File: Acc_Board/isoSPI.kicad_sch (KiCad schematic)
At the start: 11 parts, among them J2 IsoSPI

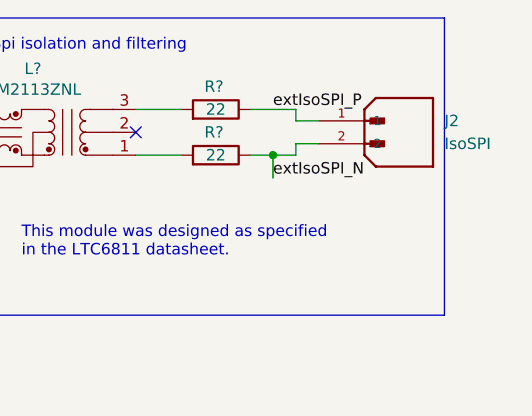
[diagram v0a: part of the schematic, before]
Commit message: Fixed crossover traces for SPI on acc board
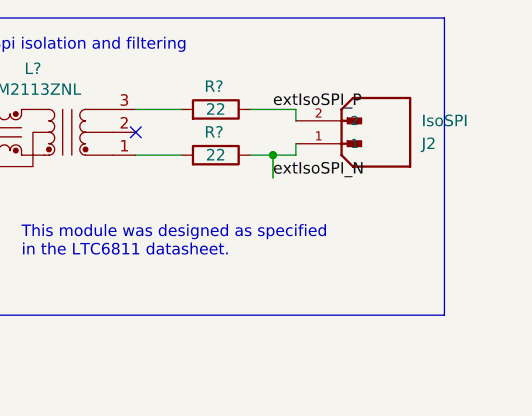
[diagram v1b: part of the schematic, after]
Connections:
- net extIsoSPI_N: now also J2.1; no longer J2.2
- net extIsoSPI_P: now also J2.2; no longer J2.1
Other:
- moved on the sheet: J2
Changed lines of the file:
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@@
-    (stroke (width 0) (type default))
-  )
-  (wire (pts (xy 166.37 33.02) (xy 168.91 33.02))
     (stroke (width 0) (type default))
   )
   (wire (pts (xy 121.92 36.83) (xy 121.92 41.91))
-    (stroke (width 0) (type default))
-  )
-  (wire (pts (xy 166.37 35.56) (xy 168.91 35.56))
     (stroke (width 0) (type default))
   )
@@
     )
   )
-  (symbol (lib_id "1FS_2_Global_Symbol_Library:1053091202") (at 173.99 33.02 0) (unit 1)
-    (in_bom yes) (on_board yes) (dnp no) (fields_autoplaced)
-    (property "Reference" "J2" (at 182.88 33.02 0)
-      (effects (font (size 1.27 1.27)) (justify left))
-    )
-    (property "Value" "IsoSPI" (at 182.88 35.56 0)
-      (effects (font (size 1.27 1.27)) (justify left))
-    )
-    (property "Footprint" "1FS_2_Global_Footprint_Library:MOLEX_1053091202" (at 173.99 33.02 0)
+  (symbol (lib_id "1FS_2_Global_Symbol_Library:1053091202") (at 171.45 35.56 0) (mirror x) (unit 1)
+    (in_bom yes) (on_board yes) (dnp no)
+    (property "Reference" "J2" (at 180.34 35.56 0)
+      (effects (font (size 1.27 1.27)) (justify left))
+    )
+    (property "Value" "IsoSPI" (at 180.34 33.02 0)
+      (effects (font (size 1.27 1.27)) (justify left))
+    )
+    (property "Footprint" "1FS_2_Global_Footprint_Library:MOLEX_1053091202" (at 171.45 35.56 0)
       (effects (font (size 1.27 1.27)) (justify bottom) hide)
     )
-    (property "Datasheet" "" (at 173.99 33.02 0)
-      (effects (font (size 1.27 1.27)) hide)
-    )
-    (property "PARTREV" "H" (at 173.99 33.02 0)
+    (property "Datasheet" "" (at 171.45 35.56 0)
+      (effects (font (size 1.27 1.27)) hide)
+    )
+    (property "PARTREV" "H" (at 171.45 35.56 0)
       (effects (font (size 1.27 1.27)) (justify bottom) hide)
     )
-    (property "STANDARD" "Manufacturer Recommendations" (at 173.99 33.02 0)
+    (property "STANDARD" "Manufacturer Recommendations" (at 171.45 35.56 0)
       (effects (font (size 1.27 1.27)) (justify bottom) hide)
     )
-    (property "MAXIMUM_PACKAGE_HEIGHT" "10.51 mm" (at 173.99 33.02 0)
+    (property "MAXIMUM_PACKAGE_HEIGHT" "10.51 mm" (at 171.45 35.56 0)
       (effects (font (size 1.27 1.27)) (justify bottom) hide)
     )
-    (property "MANUFACTURER" "Molex" (at 173.99 33.02 0)
+    (property "MANUFACTURER" "Molex" (at 171.45 35.56 0)
       (effects (font (size 1.27 1.27)) (justify bottom) hide)
     )

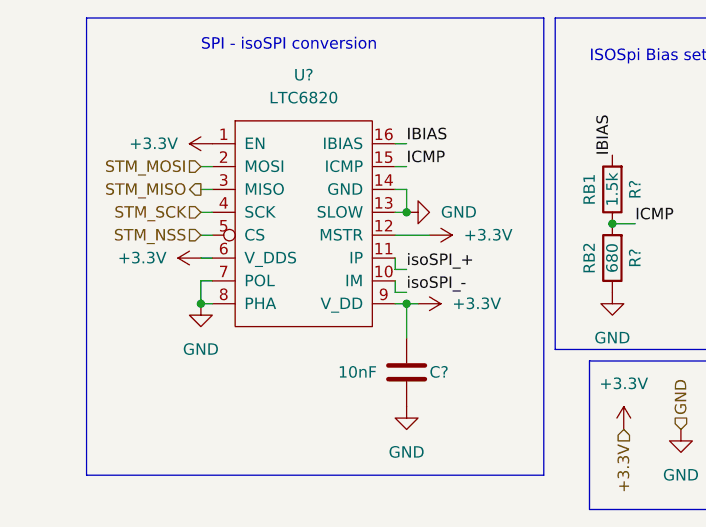
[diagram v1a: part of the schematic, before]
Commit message: acc board bms miso pull up resistor
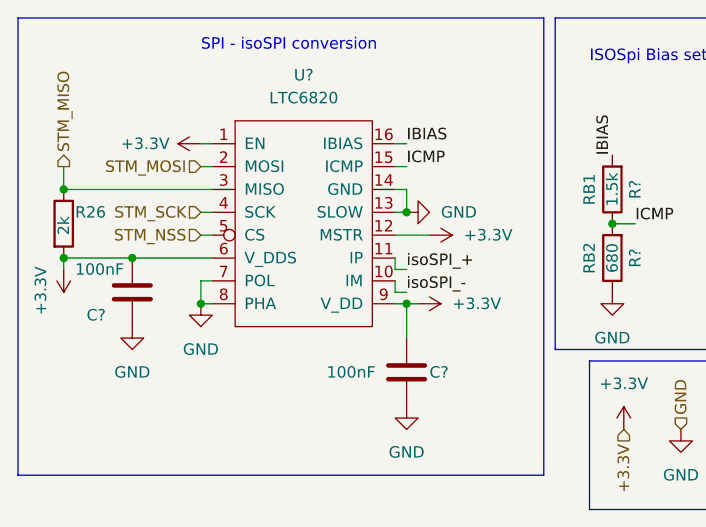
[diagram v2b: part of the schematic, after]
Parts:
- added C?: 100nF, Capacitor_SMD:C_0805_2012Metric_Pad1.18x1.45mm_HandSolder, symbol Device:C
- added R26: 2k, symbol Device:R
- C?: value 10nF -> 100nF
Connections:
- net +3.3V: now also C?.1, R26.2
- net GND: now also C?.2
- net STM_MISO: now also R26.1
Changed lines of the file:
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@@
 (kicad_sch (version 20230121) (generator eeschema)
   (paper "A4")
+  (junction (at 20.32 48.26) (diameter 0) (color 0 0 0 0)
+  )
   (junction (at 163.83 36.83) (diameter 0) (color 0 0 0 0)
   )
   (junction (at 116.84 26.67) (diameter 0) (color 0 0 0 0)
   )
+  (junction (at 20.32 40.64) (diameter 0) (color 0 0 0 0)
+  )
   (junction (at 58.42 53.34) (diameter 0) (color 0 0 0 0)
   )
@@
   )
   (junction (at 116.84 41.91) (diameter 0) (color 0 0 0 0)
+  )
+  (junction (at 27.94 48.26) (diameter 0) (color 0 0 0 0)
   )
   (no_connect (at 148.59 34.29))
@@
     (stroke (width 0) (type default))
   )
-  (wire (pts (xy 35.56 40.64) (xy 36.83 40.64))
+  (wire (pts (xy 20.32 40.64) (xy 36.83 40.64))
     (stroke (width 0) (type default))
   )
@@
     (stroke (width 0) (type default))
   )
+  (wire (pts (xy 35.56 35.56) (xy 36.83 35.56))
+    (stroke (width 0) (type default))
+  )
+  (wire (pts (xy 27.94 48.26) (xy 36.83 48.26))
+    (stroke (width 0) (type default))
+  )
   (polyline (pts (xy 101.6 54.61) (xy 101.6 21.59))
     (stroke (width 0) (type default))
@@
     (stroke (width 0) (type default))
   )
+  (wire (pts (xy 20.32 38.1) (xy 20.32 40.64))
+    (stroke (width 0) (type default))
+  )
   (wire (pts (xy 58.42 35.56) (xy 57.15 35.56))
     (stroke (width 0) (type default))
@@
     (stroke (width 0) (type default))
   )
-  (wire (pts (xy 35.56 48.26) (xy 36.83 48.26))
+  (wire (pts (xy 20.32 48.26) (xy 27.94 48.26))
     (stroke (width 0) (type default))
   )
@@
     (stroke (width 0) (type default))
   )
+  (wire (pts (xy 20.32 49.53) (xy 20.32 48.26))
+    (stroke (width 0) (type default))
+  )
   (wire (pts (xy 58.42 38.1) (xy 57.15 38.1))
     (stroke (width 0) (type default))
@@
     (stroke (width 0) (type default))
   )
-  (rectangle (start 22.86 21.59) (end 73.66 72.39)
+  (rectangle (start 15.24 21.59) (end 73.66 72.39)
     (stroke (width 0) (type default))
     (fill (type none))
@@
     (effects (font (size 1.27 1.27)) (justify right))
   )
-  (hierarchical_label "STM_MISO" (shape output) (at 35.56 40.64 180) (fields_autoplaced)
-    (effects (font (size 1.27 1.27)) (justify right))
+  (hierarchical_label "STM_MISO" (shape output) (at 20.32 38.1 90) (fields_autoplaced)
+    (effects (font (size 1.27 1.27)) (justify left))
   )
   (hierarchical_label "STM_MOSI" (shape input) (at 35.56 38.1 180) (fields_autoplaced)
@@
     )
   )
+  (symbol (lib_id "Device:C") (at 27.94 52.07 0) (unit 1)
+    (in_bom yes) (on_board yes) (dnp no)
+    (property "Reference" "C?" (at 22.86 54.61 0)
+      (effects (font (size 1.27 1.27)) (justify left))
+    )
+    (property "Value" "100nF" (at 21.59 49.53 0)
+      (effects (font (size 1.27 1.27)) (justify left))
+    )
+    (property "Footprint" "Capacitor_SMD:C_0805_2012Metric_Pad1.18x1.45mm_HandSolder" (at 28.9052 55.88 0)
+      (effects (font (size 1.27 1.27)) hide)
+    )
+    (property "Datasheet" "~" (at 27.94 52.07 0)
+      (effects (font (size 1.27 1.27)) hide)
+    )
+    (pin "1")
+    (pin "2")
+    (instances
+      (project "BMS_Controller"
+        (path "/cb6c61fd-673a-449c-8134-4a1c25621518"
+          (reference "C?") (unit 1)
+        )
+        (path "/cb6c61fd-673a-449c-8134-4a1c25621518/faa386f8-35fb-44d9-8ccf-12944498b7dc"
+          (reference "C?") (unit 1)
+        )
+      )
+      (project "Acc_Board"
+        (path "/e19d26dd-723b-45e6-9d59-b1730158e759/418586a7-bc6a-480e-8435-4a2eb96d1e0c"
+          (reference "C18") (unit 1)
+        )
+      )
+    )
+  )
   (symbol (lib_id "FSSymbols:HM2113ZNL") (at 137.16 34.29 0) (unit 1)
     (in_bom yes) (on_board yes) (dnp no)
@@
     )
   )
-  (symbol (lib_id "power:+3.3V") (at 35.56 48.26 90) (unit 1)
-    (in_bom yes) (on_board yes) (dnp no) (fields_autoplaced)
-    (property "Reference" "#PWR?" (at 39.37 48.26 0)
-      (effects (font (size 1.27 1.27)) hide)
-    )
-    (property "Value" "+3.3V" (at 31.75 48.26 90)
-      (effects (font (size 1.27 1.27)) (justify left))
-    )
-    (property "Footprint" "" (at 35.56 48.26 0)
-      (effects (font (size 1.27 1.27)) hide)
-    )
-    (property "Datasheet" "" (at 35.56 48.26 0)
+  (symbol (lib_id "power:+3.3V") (at 20.32 49.53 180) (unit 1)
+    (in_bom yes) (on_board yes) (dnp no)
+    (property "Reference" "#PWR?" (at 20.32 45.72 0)
+      (effects (font (size 1.27 1.27)) hide)
+    )
+    (property "Value" "+3.3V" (at 17.78 54.61 90)
+      (effects (font (size 1.27 1.27)) (justify right))
+    )
+    (property "Footprint" "" (at 20.32 49.53 0)
+      (effects (font (size 1.27 1.27)) hide)
+    )
+    (property "Datasheet" "" (at 20.32 49.53 0)
       (effects (font (size 1.27 1.27)) hide)
     )
@@
     )
   )
+  (symbol (lib_id "power:GND") (at 27.94 55.88 0) (unit 1)
+    (in_bom yes) (on_board yes) (dnp no) (fields_autoplaced)
+    (property "Reference" "#PWR055" (at 27.94 62.23 0)
+      (effects (font (size 1.27 1.27)) hide)
+    )
+    (property "Value" "GND" (at 27.94 60.96 0)
+      (effects (font (size 1.27 1.27)))
+    )
+    (property "Footprint" "" (at 27.94 55.88 0)
+      (effects (font (size 1.27 1.27)) hide)
+    )
+    (property "Datasheet" "" (at 27.94 55.88 0)
+      (effects (font (size 1.27 1.27)) hide)
+    )
+    (pin "1")
+    (instances
+      (project "Acc_Board"
+        (path "/e19d26dd-723b-45e6-9d59-b1730158e759/418586a7-bc6a-480e-8435-4a2eb96d1e0c"
+          (reference "#PWR055") (unit 1)
+        )
+      )
+    )
+  )
   (symbol (lib_id "Device:C") (at 58.42 60.96 0) (unit 1)
     (in_bom yes) (on_board yes) (dnp no)
@@
       (effects (font (size 1.27 1.27)) (justify left))
     )
-    (property "Value" "10nF" (at 50.8 60.96 0)
+    (property "Value" "100nF" (at 49.53 60.96 0)
       (effects (font (size 1.27 1.27)) (justify left))
     )
@@
     )
   )
-  (symbol (lib_id "power:+3.3V") (at 36.83 35.56 90) (unit 1)
-    (in_bom yes) (on_board yes) (dnp no) (fields_autoplaced)
-    (property "Reference" "#PWR?" (at 40.64 35.56 0)
-      (effects (font (size 1.27 1.27)) hide)
-    )
-    (property "Value" "+3.3V" (at 33.02 35.56 90)
-      (effects (font (size 1.27 1.27)) (justify left))
-    )
-    (property "Footprint" "" (at 36.83 35.56 0)
-      (effects (font (size 1.27 1.27)) hide)
-    )
-    (property "Datasheet" "" (at 36.83 35.56 0)
+  (symbol (lib_id "power:+3.3V") (at 35.56 35.56 90) (unit 1)
+    (in_bom yes) (on_board yes) (dnp no)
+    (property "Reference" "#PWR?" (at 39.37 35.56 0)
+      (effects (font (size 1.27 1.27)) hide)
+    )
+    (property "Value" "+3.3V" (at 26.67 35.56 90)
+      (effects (font (size 1.27 1.27)) (justify right))
+    )
+    (property "Footprint" "" (at 35.56 35.56 0)
+      (effects (font (size 1.27 1.27)) hide)
+    )
+    (property "Datasheet" "" (at 35.56 35.56 0)
       (effects (font (size 1.27 1.27)) hide)
     )
@@
         )
       )
+    )
+  )
+  (symbol (lib_id "Device:R") (at 20.32 44.45 0) (unit 1)
+    (in_bom yes) (on_board yes) (dnp no)
+    (property "Reference" "R26" (at 21.59 43.18 0)
+      (effects (font (size 1.27 1.27)) (justify left))
+    )
+    (property "Value" "2k" (at 20.32 45.72 90)
+      (effects (font (size 1.27 1.27)) (justify left))
+    )
+    (property "Footprint" "" (at 18.542 44.45 90)
+      (effects (font (size 1.27 1.27)) hide)
+    )
+    (property "Datasheet" "~" (at 20.32 44.45 0)
+      (effects (font (size 1.27 1.27)) hide)
+    )
+    (pin "2")
+    (pin "1")
+    (instances
+      (project "Acc_Board"
+        (path "/e19d26dd-723b-45e6-9d59-b1730158e759/418586a7-bc6a-480e-8435-4a2eb96d1e0c"
+          (reference "R26") (unit 1)
+        )
+      )

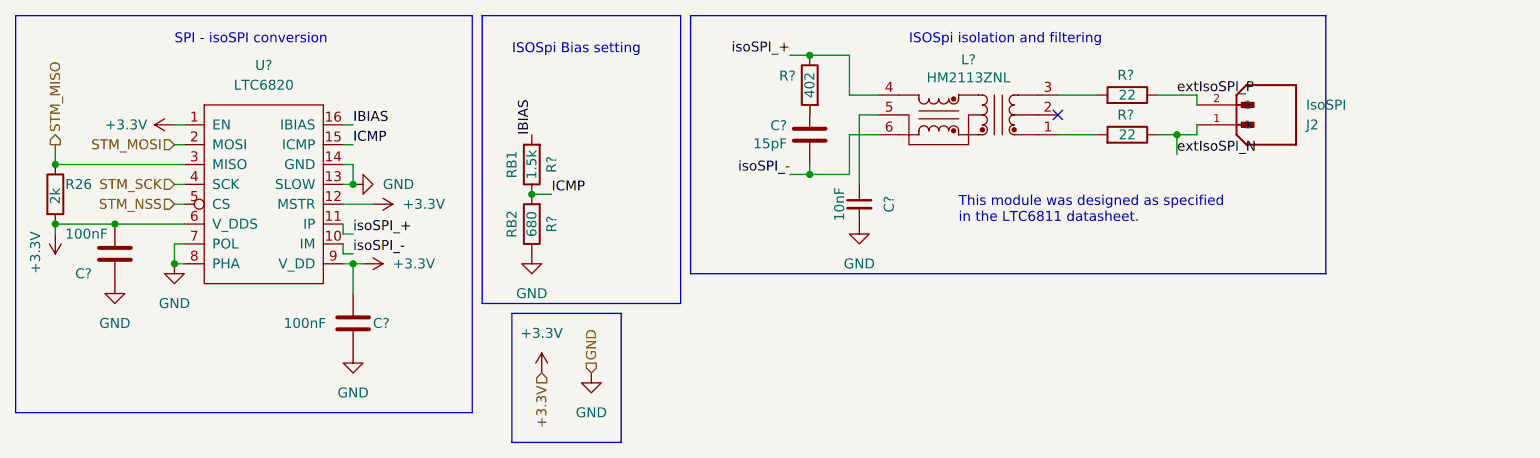
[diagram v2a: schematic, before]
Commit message: Fixed latching relay on acc board
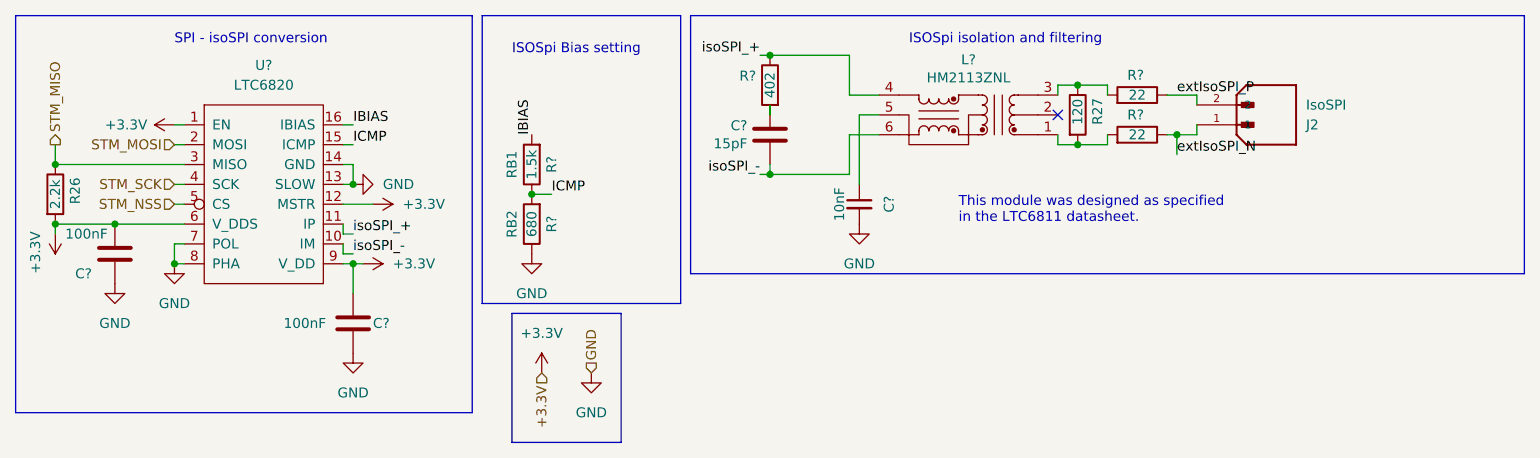
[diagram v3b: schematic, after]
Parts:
- added R27: 120, Resistor_SMD:R_0805_2012Metric_Pad1.20x1.40mm_HandSolder, symbol Device:R
- R26: value 2k -> 2.2k; footprint (none) -> Resistor_SMD:R_0805_2012Metric_Pad1.20x1.40mm_HandSolder
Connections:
- net at L?.1, R?.2: now also R27.2
- net at L?.3, R?.2: now also R27.1
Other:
- moved on the sheet: C?, R?

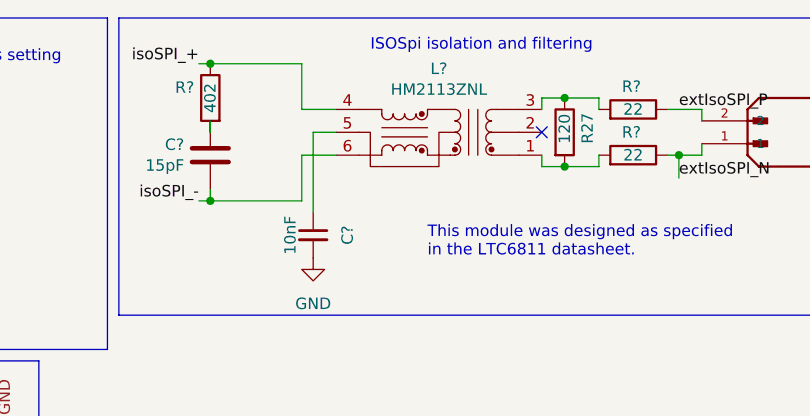
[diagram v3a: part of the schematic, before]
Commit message: Acc board SPI fixes
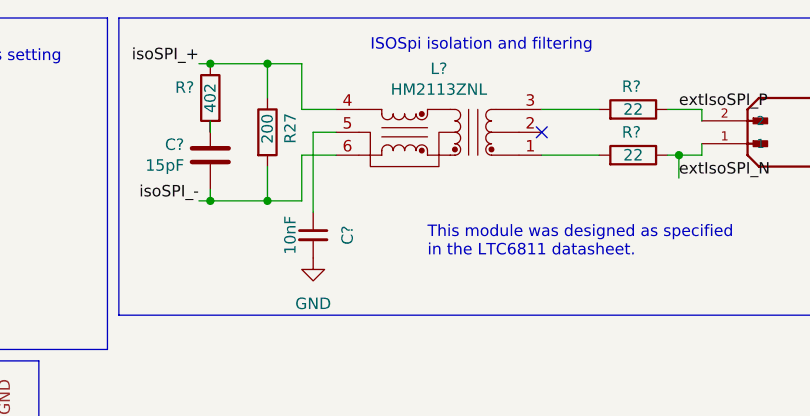
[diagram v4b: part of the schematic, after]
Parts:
- R27: value 120 -> 200
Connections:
- net isoSPI_+: now also R27.1
- net isoSPI_-: now also R27.2
- net at L?.1, R?.2: no longer R27.2
- net at L?.3, R?.2: no longer R27.1
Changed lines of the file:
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@@
 (kicad_sch (version 20230121) (generator eeschema)
   (paper "A4")
-  (junction (at 151.13 30.48) (diameter 0) (color 0 0 0 0)
-  )
-  (junction (at 151.13 38.1) (diameter 0) (color 0 0 0 0)
+  (junction (at 118.11 41.91) (diameter 0) (color 0 0 0 0)
   )
   (junction (at 20.32 48.26) (diameter 0) (color 0 0 0 0)
   )
   (junction (at 163.83 36.83) (diameter 0) (color 0 0 0 0)
+  )
+  (junction (at 118.11 26.67) (diameter 0) (color 0 0 0 0)
   )
   (junction (at 111.76 26.67) (diameter 0) (color 0 0 0 0)
@@
     (stroke (width 0) (type default))
   )
-  (wire (pts (xy 111.76 26.67) (xy 121.92 26.67))
-    (stroke (width 0) (type default))
-  )
-  (wire (pts (xy 148.59 36.83) (xy 148.59 38.1))
+  (wire (pts (xy 111.76 26.67) (xy 118.11 26.67))
+    (stroke (width 0) (type default))
+  )
+  (wire (pts (xy 118.11 26.67) (xy 118.11 30.48))
     (stroke (width 0) (type default))
   )
@@
     (stroke (width 0) (type default))
   )
-  (wire (pts (xy 154.94 30.48) (xy 154.94 31.75))
-    (stroke (width 0) (type default))
-  )
   (wire (pts (xy 35.56 45.72) (xy 36.83 45.72))
     (stroke (width 0) (type default))
@@
     (stroke (width 0) (type default))
   )
+  (wire (pts (xy 118.11 38.1) (xy 118.11 41.91))
+    (stroke (width 0) (type default))
+  )
   (wire (pts (xy 58.42 53.34) (xy 57.15 53.34))
     (stroke (width 0) (type default))
@@
     (stroke (width 0) (type default))
   )
-  (wire (pts (xy 154.94 36.83) (xy 154.94 38.1))
-    (stroke (width 0) (type default))
-  )
   (wire (pts (xy 121.92 36.83) (xy 125.73 36.83))
     (stroke (width 0) (type default))
@@
     (stroke (width 0) (type default))
   )
-  (wire (pts (xy 151.13 30.48) (xy 154.94 30.48))
-    (stroke (width 0) (type default))
-  )
-  (wire (pts (xy 148.59 30.48) (xy 148.59 31.75))
+  (wire (pts (xy 148.59 31.75) (xy 154.94 31.75))
     (stroke (width 0) (type default))
   )
@@
     (stroke (width 0) (type default))
   )
+  (wire (pts (xy 118.11 41.91) (xy 121.92 41.91))
+    (stroke (width 0) (type default))
+  )
   (wire (pts (xy 57.15 40.64) (xy 58.42 40.64))
     (stroke (width 0) (type default))
@@
     (stroke (width 0) (type default))
   )
-  (wire (pts (xy 151.13 38.1) (xy 148.59 38.1))
-    (stroke (width 0) (type default))
-  )
   (wire (pts (xy 121.92 26.67) (xy 121.92 31.75))
     (stroke (width 0) (type default))
@@
     (stroke (width 0) (type default))
   )
-  (wire (pts (xy 148.59 30.48) (xy 151.13 30.48))
-    (stroke (width 0) (type default))
-  )
   (wire (pts (xy 35.56 38.1) (xy 36.83 38.1))
     (stroke (width 0) (type default))
@@
     (stroke (width 0) (type default))
   )
-  (wire (pts (xy 154.94 38.1) (xy 151.13 38.1))
-    (stroke (width 0) (type default))
-  )
-  (wire (pts (xy 111.76 41.91) (xy 121.92 41.91))
+  (wire (pts (xy 148.59 36.83) (xy 154.94 36.83))
+    (stroke (width 0) (type default))
+  )
+  (wire (pts (xy 118.11 26.67) (xy 121.92 26.67))
+    (stroke (width 0) (type default))
+  )
+  (wire (pts (xy 111.76 41.91) (xy 118.11 41.91))
     (stroke (width 0) (type default))
   )
@@
         (path "/e19d26dd-723b-45e6-9d59-b1730158e759/418586a7-bc6a-480e-8435-4a2eb96d1e0c"
           (reference "#PWR037") (unit 1)
+        )
+      )
+    )
+  )
+  (symbol (lib_id "Device:R") (at 118.11 34.29 0) (unit 1)
+    (in_bom yes) (on_board yes) (dnp no)
+    (property "Reference" "R27" (at 120.65 35.56 90)
+      (effects (font (size 1.27 1.27)) (justify left))
+    )
+    (property "Value" "200" (at 118.11 35.56 90)
+      (effects (font (size 1.27 1.27)) (justify left))
+    )
+    (property "Footprint" "Resistor_SMD:R_0805_2012Metric_Pad1.20x1.40mm_HandSolder" (at 116.332 34.29 90)
+      (effects (font (size 1.27 1.27)) hide)
+    )
+    (property "Datasheet" "~" (at 118.11 34.29 0)
+      (effects (font (size 1.27 1.27)) hide)
+    )
+    (pin "1")
+    (pin "2")
+    (instances
+      (project "Acc_Board"
+        (path "/e19d26dd-723b-45e6-9d59-b1730158e759/418586a7-bc6a-480e-8435-4a2eb96d1e0c"
+          (reference "R27") (unit 1)
         )
       )
@@
         )
       )
-    )
-  )
-  (symbol (lib_id "Device:R") (at 151.13 34.29 0) (unit 1)
-    (in_bom yes) (on_board yes) (dnp no)
-    (property "Reference" "R27" (at 153.67 35.56 90)
-      (effects (font (size 1.27 1.27)) (justify left))
-    )
-    (property "Value" "120" (at 151.13 35.56 90)
-      (effects (font (size 1.27 1.27)) (justify left))
-    )
-    (property "Footprint" "Resistor_SMD:R_0805_2012Metric_Pad1.20x1.40mm_HandSolder" (at 149.352 34.29 90)
-      (effects (font (size 1.27 1.27)) hide)
-    )
-    (property "Datasheet" "~" (at 151.13 34.29 0)
-      (effects (font (size 1.27 1.27)) hide)
-    )
-    (pin "1")
-    (pin "2")
-    (instances
-      (project "Acc_Board"
-        (path "/e19d26dd-723b-45e6-9d59-b1730158e759/418586a7-bc6a-480e-8435-4a2eb96d1e0c"
-          (reference "R27") (unit 1)
-        )
-      )
